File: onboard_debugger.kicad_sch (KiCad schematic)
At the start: 23 parts, among them J3 USB_C_Receptacle_USB2.0_16P, J5 Conn_01x05, SW3 SW_Push, U3 USBLC6-2SC6, U4 STM32F103C8Tx, U5 AMS1117-3.3, Y2 8MHz

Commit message: fix: adjust the wiring label
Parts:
- added C23: 100nF, symbol Device:C
- R5: renamed from R7; value R -> 10K
- renumbered C17 to C19, C27 to C20, C28 to C21, C18 to C22, C21 to C24, C22 to C25, C23 to C26, C24 to C27, C25 to C28, C26 to C29, F_DBG_USB to F_DBG_USB1, J3 to J2, J5 to J3, R2 to R4, R5 to R6, R4 to R7, SW3 to SW2, U5 to U3, U3 to U4, U4 to U5
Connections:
- net DH0_DBG is gone; now on net PH0_DBG: U5.5 (PD0)
- net DH1_DBG is gone; now on net PH1_DBG: U5.6 (PD1)
- net DBG_SWCLK: now also J3.3 (Pin_3)
- net DBG_SWDIO: now also J3.2 (Pin_2)
- net GND: now also C23.1
- net SWCLK: no longer J3.3 (Pin_3)
- net SWDIO: no longer J3.2 (Pin_2)
- net VBUS_DBG_RAW: now also F_DBG_USB1.1, J2.A4 (VBUS), J2.A9 (VBUS), J2.B4 (VBUS), J2.B9 (VBUS), C23.2
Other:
- moved on the sheet: F_DBG_USB1

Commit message: fix: revise power supply and onboard debug circuitry
Separate power sheet, add dual buck regulation and USB/DC isolation, and add debug isolation jumpers, programming headers and target reset. Include schematic PDF, ERC report and remaining validation requirements.
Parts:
- added C36: 100nF, Capacitor_SMD:C_0805_2012Metric, symbol Device:C
- added J4: F103 PROGRAMMING, Connector_PinHeader_2.54mm:PinHeader_1x06_P2.54mm_Vertical, symbol Connector_Generic:Conn_01x06
- added J5: TARGET TRACE UART, Connector_PinHeader_2.54mm:PinHeader_1x06_P2.54mm_Vertical, symbol Connector_Generic:Conn_01x06
- added JP2: DBG_SWDIO, Connector_PinHeader_2.54mm:PinHeader_1x02_P2.54mm_Vertical, symbol Jumper:Jumper_2_Open
- added JP3: DBG_SWCLK, Connector_PinHeader_2.54mm:PinHeader_1x02_P2.54mm_Vertical, symbol Jumper:Jumper_2_Open
- added JP4: DBG_T_NRST, Connector_PinHeader_2.54mm:PinHeader_1x02_P2.54mm_Vertical, symbol Jumper:Jumper_2_Open
- added R8: 10k, Resistor_SMD:R_0805_2012Metric, symbol Device:R
- added SW3: TARGET RESET, Button_Switch_THT:SW_PUSH_6mm, symbol Switch:SW_Push
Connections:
- net +3.3V: now also J5.1 (Pin_1), R8.1
- net +3V3_DBG: now also J4.1 (Pin_1)
- net DBG_SWCLK: now also JP3.2 (B); no longer U5.45 (PB8)
- net DBG_SWDIO: now also JP2.2 (B); no longer U5.43 (PB7)
- net DBG_T_NRST: now also C36.1, J5.6 (Pin_6), JP4.2 (B), R8.2, SW3.1; no longer U5.46 (PB9)
- net GND: now also C36.2, J4.3 (Pin_3), J5.3 (Pin_3), SW3.2
- net NRST_DBG: now also J4.5 (Pin_5)
- net SWCLK renamed F103_SWCLK
- net F103_SWCLK: now also J4.4 (Pin_4)
- net SWDIO renamed F103_SWDIO
- net F103_SWDIO: now also J4.2 (Pin_2)
- new net ONB_DBG_SWCLK: JP3.1 (A), U5.45 (PB8)
- new net ONB_DBG_SWDIO: JP2.1 (A), U5.43 (PB7)
- new net ONB_DBG_T_NRST: JP4.1 (A), U5.46 (PB9)
- new net TARGET_RX: J5.5 (Pin_5)
- new net TARGET_SWO: J5.2 (Pin_2)
- new net TARGET_TX: J5.4 (Pin_4)
- no-connect marks 2 -> 3
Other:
- note added: "DEBUG ACCESS / ISOLATION - CMSIS-DAP firmware pin mapping must match PB7 / PB8 / PB9."
- note added: "J4 pin1 / J5 pin1 are voltage references, NOT inputs for a second power supply."
- note added: "J5: SWO=F407 PB3; TX=PD8, RX=PD9 (USART3). No unverified connection to F103 firmware."
- note added: "JP2-4: fit only for onboard debug with BOTH rails powered; remove for external probe or unpowered target."

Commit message: Revert "fix: revise power supply and onboard debug circuitry"
This reverts commit 2d890f2299649650f44a02df67d759df60ae0ebd.
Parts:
- removed C36: 100nF, Capacitor_SMD:C_0805_2012Metric, symbol Device:C
- removed J4: F103 PROGRAMMING, Connector_PinHeader_2.54mm:PinHeader_1x06_P2.54mm_Vertical, symbol Connector_Generic:Conn_01x06
- removed J5: TARGET TRACE UART, Connector_PinHeader_2.54mm:PinHeader_1x06_P2.54mm_Vertical, symbol Connector_Generic:Conn_01x06
- removed JP2: DBG_SWDIO, Connector_PinHeader_2.54mm:PinHeader_1x02_P2.54mm_Vertical, symbol Jumper:Jumper_2_Open
- removed JP3: DBG_SWCLK, Connector_PinHeader_2.54mm:PinHeader_1x02_P2.54mm_Vertical, symbol Jumper:Jumper_2_Open
- removed JP4: DBG_T_NRST, Connector_PinHeader_2.54mm:PinHeader_1x02_P2.54mm_Vertical, symbol Jumper:Jumper_2_Open
- removed R8: 10k, Resistor_SMD:R_0805_2012Metric, symbol Device:R
- removed SW3: TARGET RESET, Button_Switch_THT:SW_PUSH_6mm, symbol Switch:SW_Push
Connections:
- net ONB_DBG_SWCLK is gone; now on net DBG_SWCLK: U5.45 (PB8)
- net ONB_DBG_SWDIO is gone; now on net DBG_SWDIO: U5.43 (PB7)
- net ONB_DBG_T_NRST is gone; now on net DBG_T_NRST: U5.46 (PB9)
- net F103_SWCLK renamed SWCLK
- net F103_SWDIO renamed SWDIO
- no-connect marks 3 -> 2
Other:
- note removed: "DEBUG ACCESS / ISOLATION - CMSIS-DAP firmware pin mapping must match PB7 / PB8 / PB9."
- note removed: "J4 pin1 / J5 pin1 are voltage references, NOT inputs for a second power supply."
- note removed: "J5: SWO=F407 PB3; TX=PD8, RX=PD9 (USART3). No unverified connection to F103 firmware."
- note removed: "JP2-4: fit only for onboard debug with BOTH rails powered; remove for external probe or unpowered target."

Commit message: refactor: add the new buck converter 12V
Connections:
- net +5V_DBG_USB: no longer C19.1, U3.3 (VI)
- new net +5V_SYS: C19.1, U3.3 (VI)

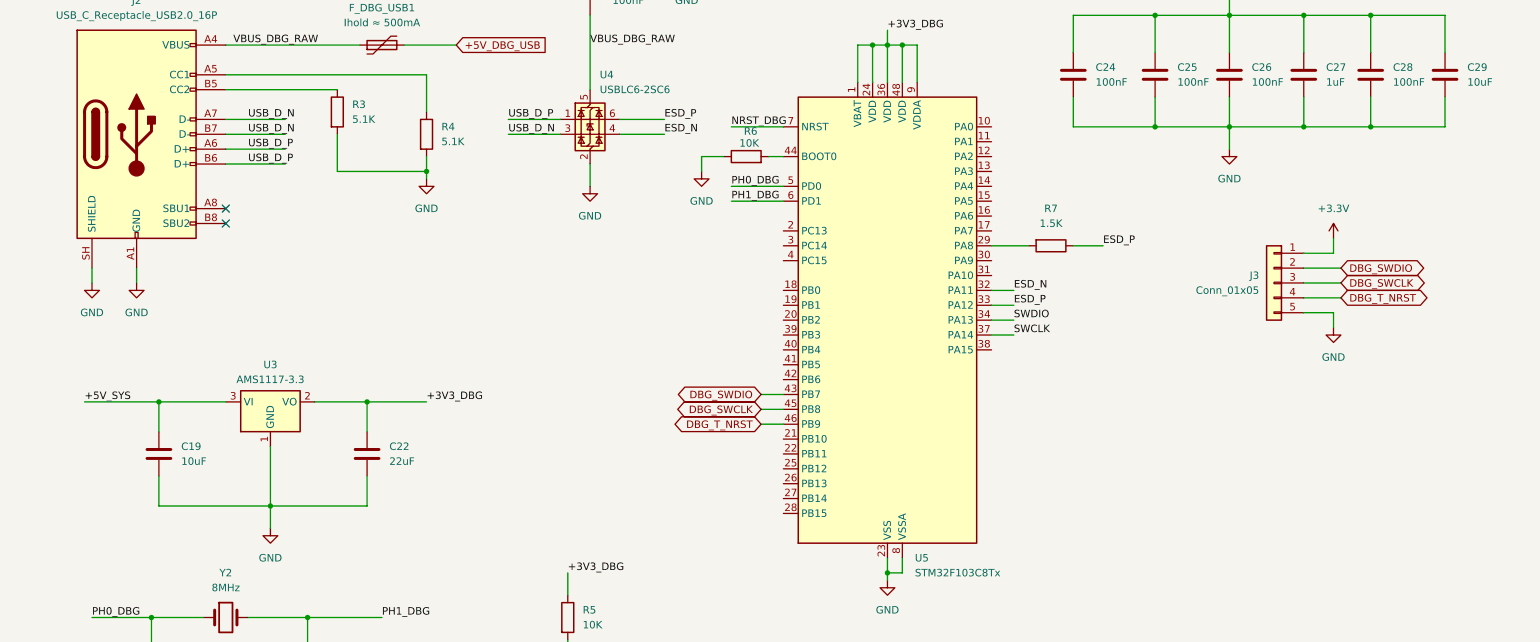
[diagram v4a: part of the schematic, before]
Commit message: feat: add the basic io schematic
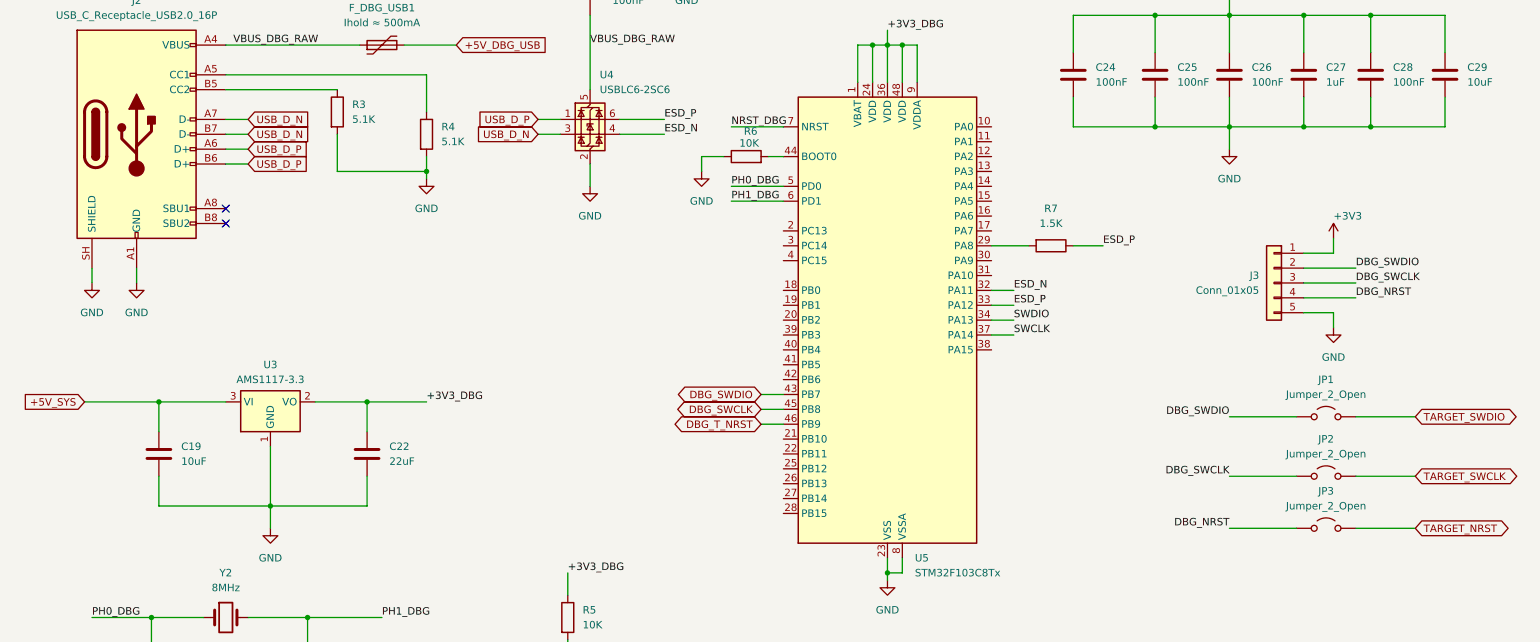
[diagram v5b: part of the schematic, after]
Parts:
- added JP1, JP2, JP3: Jumper_2_Open, symbol Jumper:Jumper_2_Open
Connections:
- net DBG_SWCLK: now also JP2.1 (A)
- net DBG_SWDIO: now also JP1.1 (A)
- net DBG_T_NRST: no longer J3.4 (Pin_4)
- net +3.3V renamed +3V3
- new net DBG_NRST: J3.4 (Pin_4), JP3.1 (A)
- new net TARGET_NRST: JP3.2 (B)
- new net TARGET_SWCLK: JP2.2 (B)
- new net TARGET_SWDIO: JP1.2 (B)

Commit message: feat: implement sensors schematic
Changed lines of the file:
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@@
-	(wire
-		(pts
-			(xy 52.07 54.61) (xy 55.88 54.61)
-		)
-		(stroke
-			(width 0)
-			(type default)
-		)
-	)
 	(wire
 		(pts
@@
 	(wire
 		(pts
-			(xy 52.07 49.53) (xy 55.88 49.53)
+			(xy 52.07 49.53) (xy 62.23 49.53)
 		)
 		(stroke
@@
 	(wire
 		(pts
+			(xy 100.33 46.99) (xy 109.22 46.99)
+		)
+		(stroke
+			(width 0)
+			(type default)
+		)
+	)
+	(wire
+		(pts
 			(xy 210.82 48.26) (xy 210.82 43.18)
 		)
@@
 	(wire
 		(pts
-			(xy 52.07 52.07) (xy 55.88 52.07)
-		)
-		(stroke
-			(width 0)
-			(type default)
-		)
-	)
-	(wire
-		(pts
 			(xy 170.18 34.29) (xy 167.64 34.29)
 		)
@@
 	(wire
 		(pts
+			(xy 52.07 46.99) (xy 62.23 46.99)
+		)
+		(stroke
+			(width 0)
+			(type default)
+		)
+	)
+	(wire
+		(pts
 			(xy 52.07 41.91) (xy 71.12 41.91)
 		)
@@
 	(wire
 		(pts
+			(xy 52.07 54.61) (xy 62.23 54.61)
+		)
+		(stroke
+			(width 0)
+			(type default)
+		)
+	)
+	(wire
+		(pts
 			(xy 36.83 72.39) (xy 36.83 74.93)
 		)
@@
 	(wire
 		(pts
-			(xy 105.41 49.53) (xy 109.22 49.53)
-		)
-		(stroke
-			(width 0)
-			(type default)
-		)
-	)
-	(wire
-		(pts
 			(xy 110.49 140.97) (xy 110.49 144.78)
 		)
@@
 	(wire
 		(pts
-			(xy 52.07 46.99) (xy 55.88 46.99)
-		)
-		(stroke
-			(width 0)
-			(type default)
-		)
-	)
-	(wire
-		(pts
 			(xy 48.26 132.08) (xy 39.37 132.08)
 		)
@@
 	(wire
 		(pts
+			(xy 100.33 49.53) (xy 109.22 49.53)
+		)
+		(stroke
+			(width 0)
+			(type default)
+		)
+	)
+	(wire
+		(pts
 			(xy 196.85 29.21) (xy 210.82 29.21)
 		)
@@
 	(wire
 		(pts
+			(xy 52.07 52.07) (xy 62.23 52.07)
+		)
+		(stroke
+			(width 0)
+			(type default)
+		)
+	)
+	(wire
+		(pts
 			(xy 39.37 132.08) (xy 39.37 138.43)
 		)
@@
 		(pts
 			(xy 138.43 60.96) (xy 147.32 60.96)
-		)
-		(stroke
-			(width 0)
-			(type default)
-		)
-	)
-	(wire
-		(pts
-			(xy 105.41 46.99) (xy 109.22 46.99)
 		)
 		(stroke
@@
 		)
 	)
+	(label "USB_D_N"
+		(at 100.33 49.53 0)
+		(effects
+			(font
+				(size 1.27 1.27)
+			)
+			(justify left bottom)
+		)
+	)
+	(label "USB_D_N"
+		(at 55.88 49.53 0)
+		(effects
+			(font
+				(size 1.27 1.27)
+			)
+			(justify left bottom)
+		)
+	)
+	(label "USB_D_P"
+		(at 55.88 52.07 0)
+		(effects
+			(font
+				(size 1.27 1.27)
+			)
+			(justify left bottom)
+		)
+	)
 	(label "SWDIO"
 		(at 186.69 81.28 0)
@@
 		)
 	)
+	(label "USB_D_N"
+		(at 55.88 46.99 0)
+		(effects
+			(font
+				(size 1.27 1.27)
+			)
+			(justify left bottom)
+		)
+	)
 	(label "VBUS_DBG_RAW"
 		(at 114.3 34.29 0)
@@
 		)
 	)
+	(label "USB_D_P"
+		(at 100.33 46.99 0)
+		(effects
+			(font
+				(size 1.27 1.27)
+			)
+			(justify left bottom)
+		)
+	)
 	(label "+3V3_DBG"
 		(at 165.1 31.75 0)
+		(effects
+			(font
+				(size 1.27 1.27)
+			)
+			(justify left bottom)
+		)
+	)
+	(label "USB_D_P"
+		(at 55.88 54.61 0)
 		(effects
 			(font
@@
 		)
 	)
-	(global_label "USB_D_P"
-		(shape input)
-		(at 55.88 54.61 0)
-		(fields_autoplaced yes)
-		(effects
-			(font
-				(size 1.27 1.27)
-			)
-			(justify left)
-		)
-		(property "Intersheetrefs" "${INTERSHEET_REFS}"
-			(at 67.1504 54.61 0)
-			(hide yes)
-			(show_name no)
-			(do_not_autoplace no)
-			(effects
-				(font
-					(size 1.27 1.27)
-				)
-				(justify left)
-			)
-		)
-	)
-	(global_label "USB_D_N"
-		(shape input)
-		(at 105.41 49.53 180)
-		(fields_autoplaced yes)
-		(effects
-			(font
-				(size 1.27 1.27)
-			)
-			(justify right)
-		)
-		(property "Intersheetrefs" "${INTERSHEET_REFS}"
-			(at 94.0791 49.53 0)
-			(hide yes)
-			(show_name no)
-			(do_not_autoplace no)
-			(effects
-				(font
-					(size 1.27 1.27)
-				)
-				(justify right)
-			)
-		)
-	)
 	(global_label "DBG_T_NRST"
 		(shape bidirectional)
@@
 		)
 	)
-	(global_label "USB_D_P"
-		(shape input)
-		(at 105.41 46.99 180)
-		(fields_autoplaced yes)
-		(effects
-			(font
-				(size 1.27 1.27)
-			)
-			(justify right)
-		)
-		(property "Intersheetrefs" "${INTERSHEET_REFS}"
-			(at 94.1396 46.99 0)
-			(hide yes)
-			(show_name no)
-			(do_not_autoplace no)
-			(effects
-				(font
-					(size 1.27 1.27)
-				)
-				(justify right)
-			)
-		)
-	)
-	(global_label "USB_D_N"
-		(shape input)
-		(at 55.88 49.53 0)
-		(fields_autoplaced yes)
-		(effects
-			(font
-				(size 1.27 1.27)
-			)
-			(justify left)
-		)
-		(property "Intersheetrefs" "${INTERSHEET_REFS}"
-			(at 67.2109 49.53 0)
-			(hide yes)
-			(show_name no)
-			(do_not_autoplace no)
-			(effects
-				(font
-					(size 1.27 1.27)
-				)
-				(justify left)
-			)
-		)
-	)
-	(global_label "USB_D_N"
-		(shape input)
-		(at 55.88 46.99 0)
-		(fields_autoplaced yes)
-		(effects
-			(font
-				(size 1.27 1.27)
-			)
-			(justify left)
-		)
-		(property "Intersheetrefs" "${INTERSHEET_REFS}"
-			(at 67.2109 46.99 0)
-			(hide yes)
-			(show_name no)
-			(do_not_autoplace no)
-			(effects
-				(font
-					(size 1.27 1.27)
-				)
-				(justify left)
-			)
-		)
-	)
 	(global_label "DBG_SWCLK"
 		(shape bidirectional)
@@
 			(hide yes)
 			(show_name no)
-			(do_not_autoplace no)
-			(effects
-				(font
-					(size 1.27 1.27)
-				)
-				(justify left)
-			)
-		)
-	)
-	(global_label "USB_D_P"
-		(shape input)
-		(at 55.88 52.07 0)
-		(fields_autoplaced yes)
-		(effects
-			(font
-				(size 1.27 1.27)
-			)
-			(justify left)
-		)
-		(property "Intersheetrefs" "${INTERSHEET_REFS}"
-			(at 67.1504 52.07 0)
-			(hide yes)
-			(show_name no)

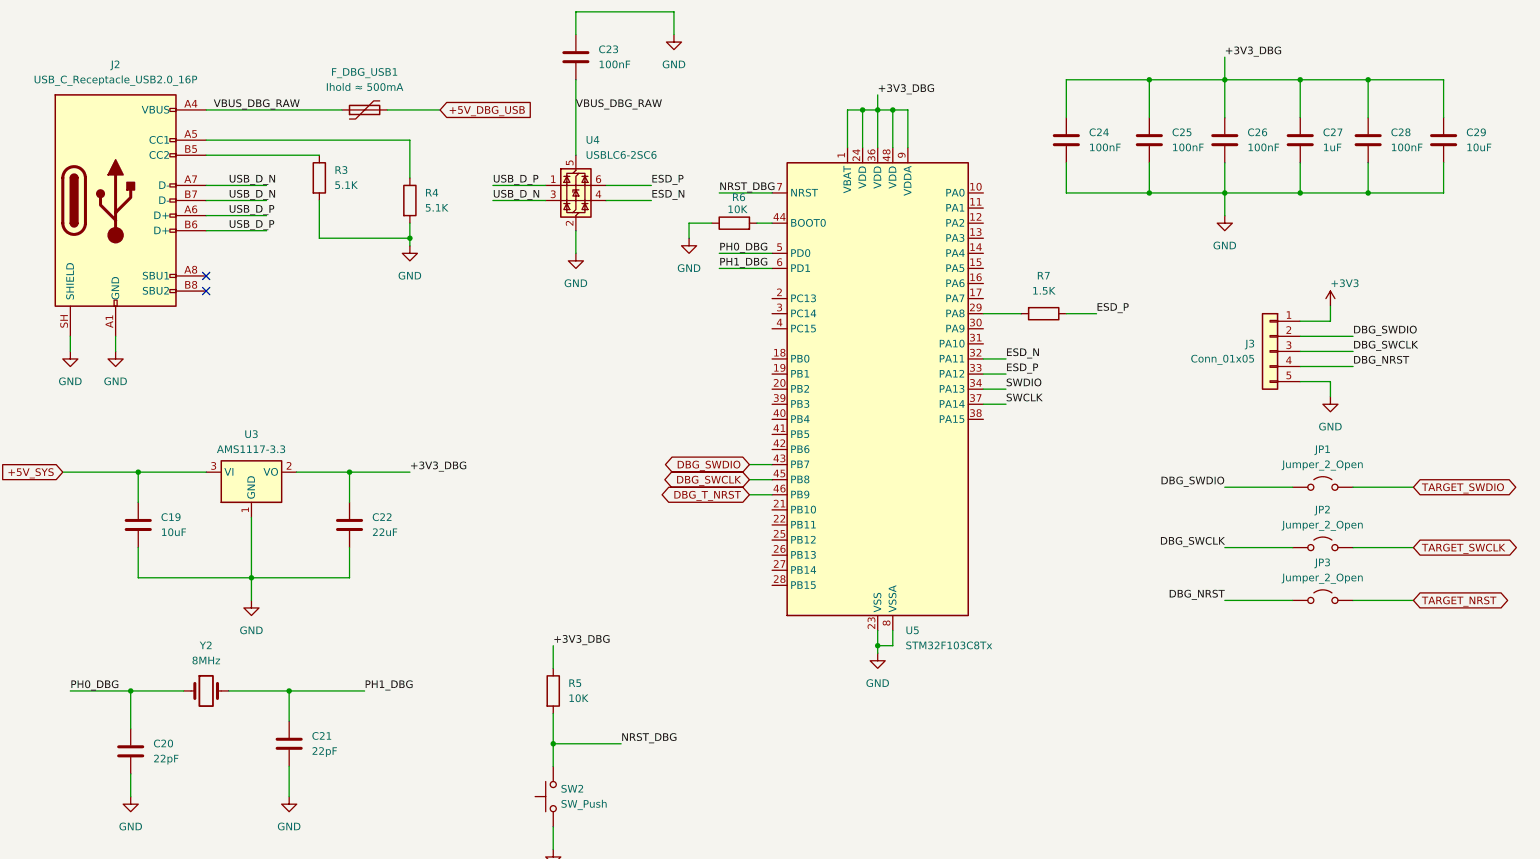
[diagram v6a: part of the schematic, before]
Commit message: feat: implement microSD schematic
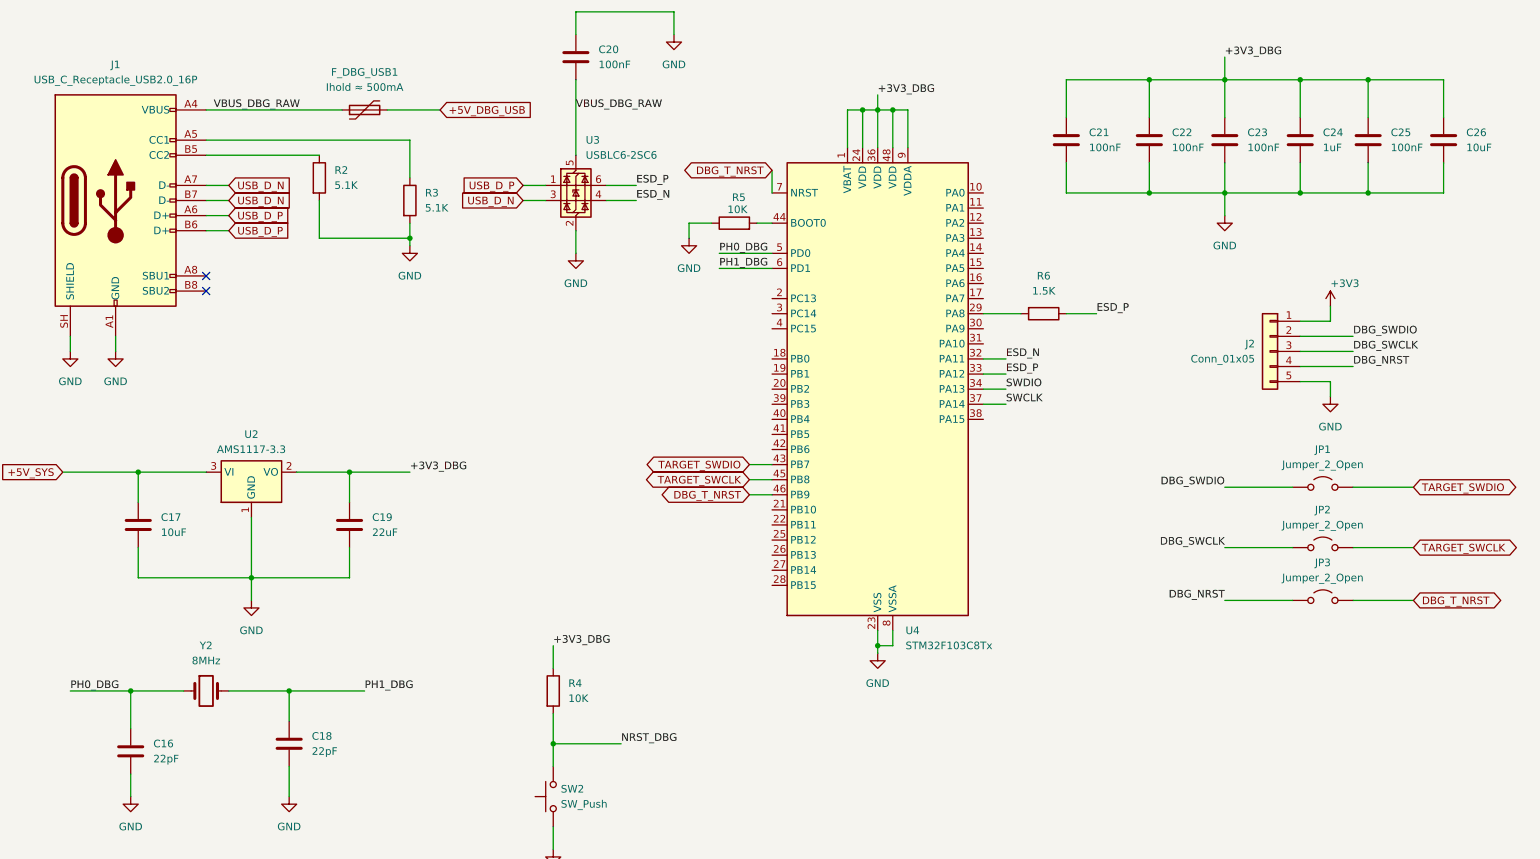
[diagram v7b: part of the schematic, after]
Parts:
- renumbered C20 to C16, C19 to C17, C21 to C18, C22 to C19, C23 to C20, C24 to C21, C25 to C22, C26 to C23, C27 to C24, C28 to C25, C29 to C26, J2 to J1, J3 to J2, R3 to R2, R4 to R3, R5 to R4, R6 to R5, R7 to R6, U3 to U2, U4 to U3, U5 to U4
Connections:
- net TARGET_NRST is gone; now on net DBG_T_NRST: JP3.2 (B)
- net DBG_SWCLK: no longer U4.45 (PB8)
- net DBG_SWDIO: no longer U4.43 (PB7)
- net DBG_T_NRST: now also U4.7 (NRST)
- net NRST_DBG: no longer U4.7 (NRST)
- net TARGET_SWCLK: now also U4.45 (PB8)
- net TARGET_SWDIO: now also U4.43 (PB7)
